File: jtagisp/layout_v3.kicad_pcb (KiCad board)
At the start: 2 copper layers, 6 parts

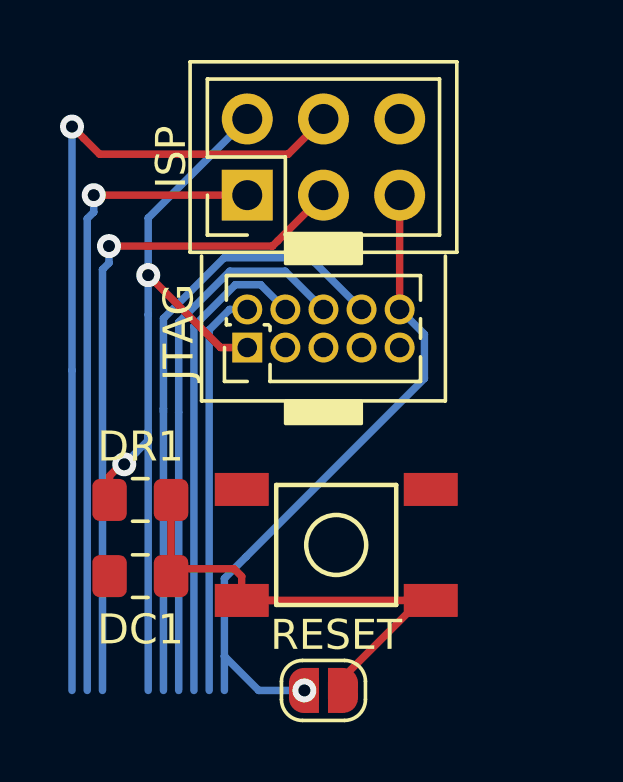
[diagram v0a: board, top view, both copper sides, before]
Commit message: Defining areas and connections per 'module'
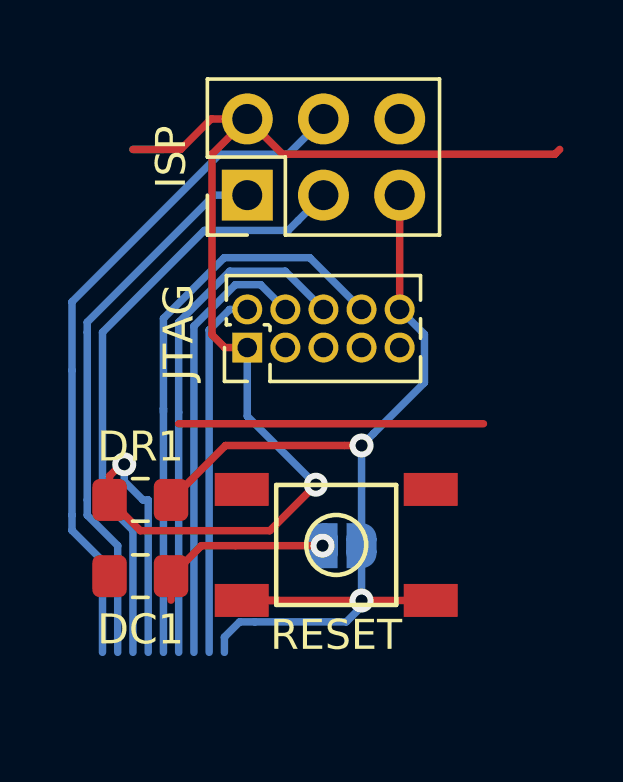
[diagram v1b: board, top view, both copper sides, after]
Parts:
- DJP1: moved to B.Cu
- moved DJP1 4.87 mm to (156.8, 67.6), turned to 180 degrees
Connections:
- DR1 pad 2: Net-(DC1-Pad2) -> ~RESET
- DSW1 pad 1: Net-(DC1-Pad2) -> ~RESET
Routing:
- net VDD: track 27.8 -> 46.1 mm
- net ~RESET: track 22.8 -> 36.3 mm, vias 1 -> 2
- net Net-(DC1-Pad2): track 18.4 -> 6.27 mm, vias 0 -> 1
- net (no net): track 0.00 -> 11.2 mm
- net MOSI: track 28.0 -> 23.0 mm, vias 1 -> 0
- net MISO: track 21.7 -> 18.5 mm, vias 1 -> 0
- net SCK: track 22.8 -> 20.3 mm, vias 1 -> 0
- net TCK: track 16.1 -> 14.8 mm
- net TMS: track 13.6 -> 12.3 mm
- net TDO: track 18.3 -> 17.1 mm
- net TDI: track 20.7 -> 19.4 mm
